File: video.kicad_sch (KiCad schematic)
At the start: 41 parts

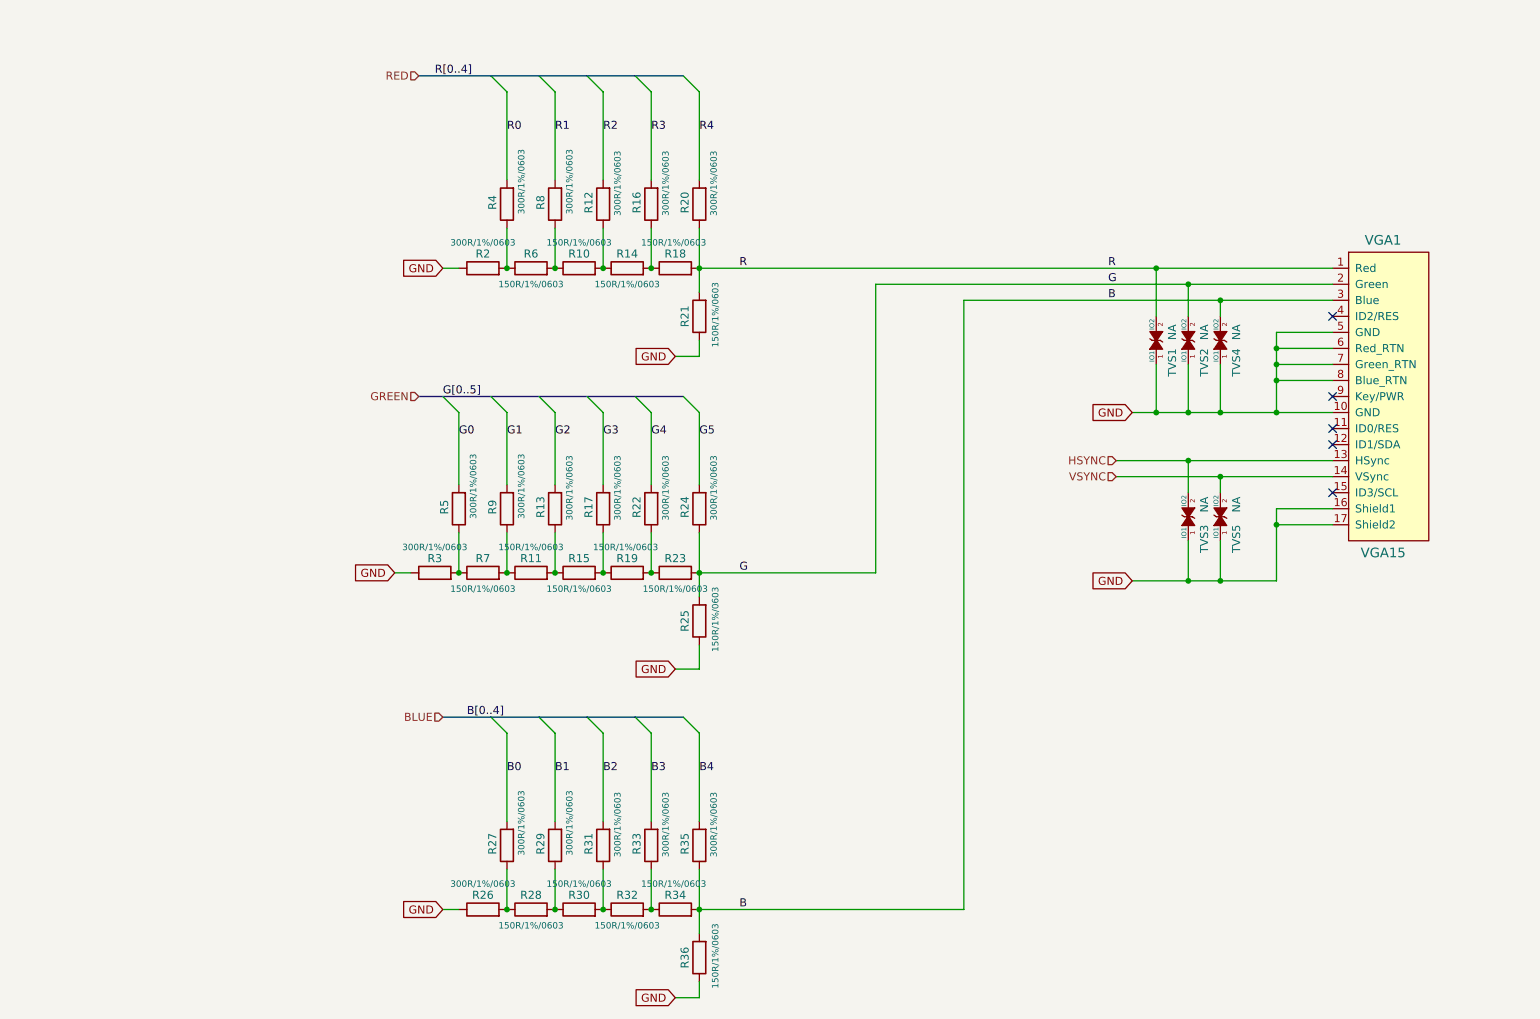
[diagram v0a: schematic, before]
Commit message: schematics finished, pcb routing 80%
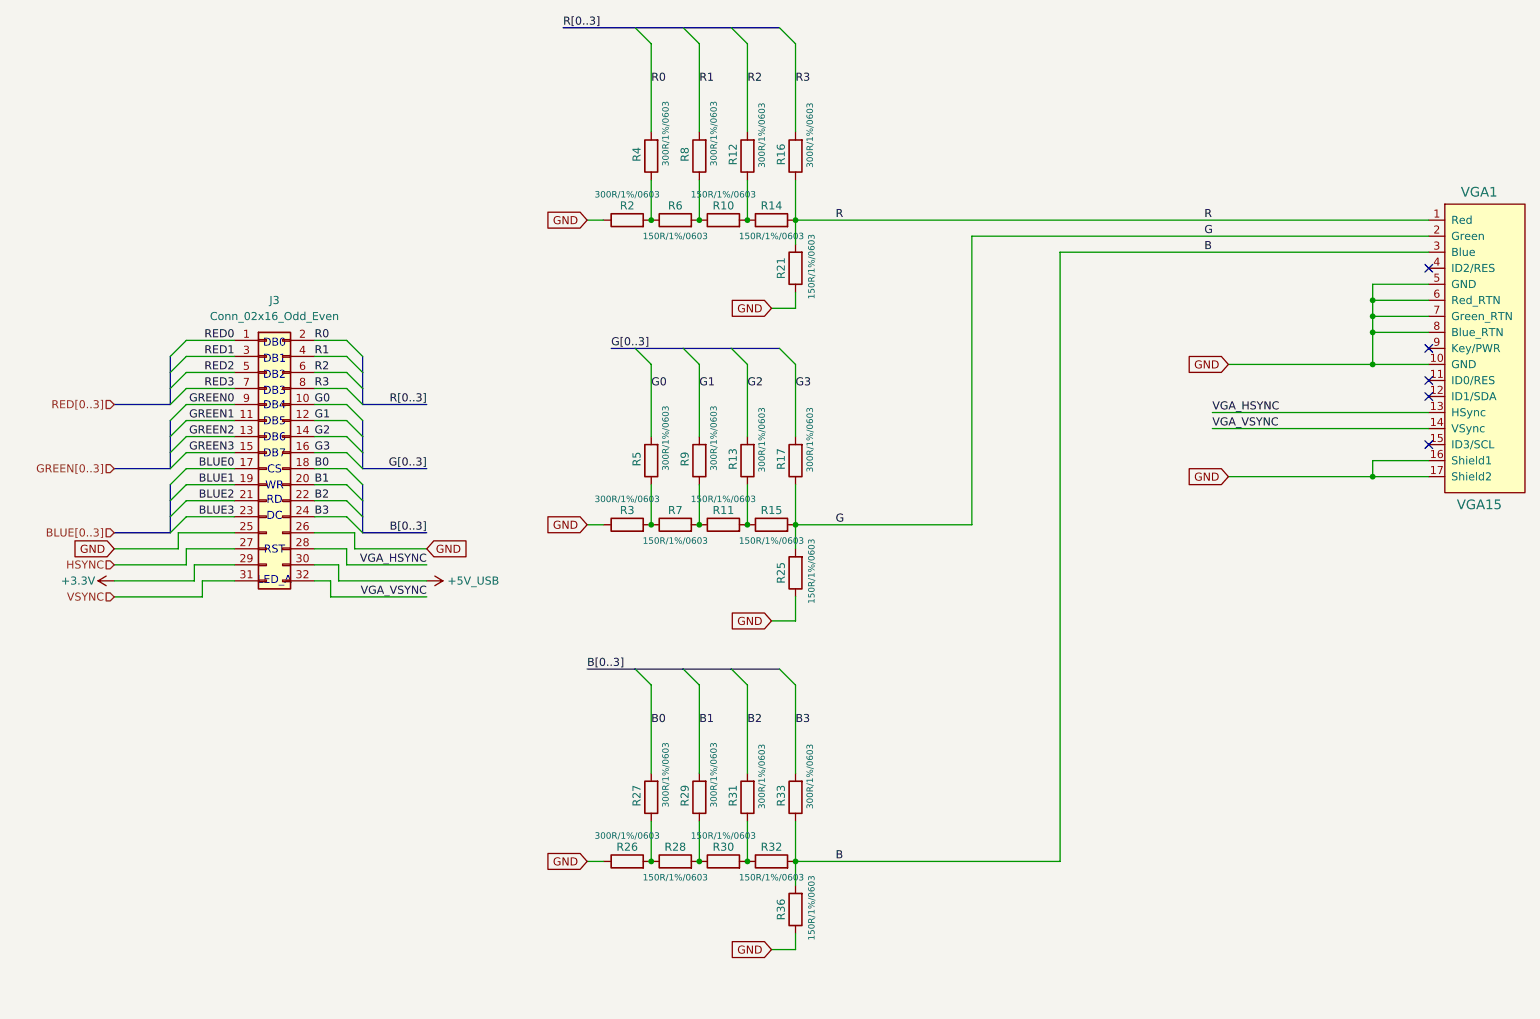
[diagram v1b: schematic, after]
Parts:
- removed R18, R19, R23, R34: 150R/1%/0603, OLIMEX_RLC-FP:R_0603_5MIL_DWS, symbol AgonLight2_Rev_B:R
- removed R20, R22, R24, R35: 300R/1%/0603, OLIMEX_RLC-FP:R_0603_5MIL_DWS, symbol AgonLight2_Rev_B:R
- removed TVS1, TVS2, TVS3, TVS4, TVS5: NA, OLIMEX_Diodes-FP:D_0402_5MIL_DWS, symbol AgonLight2_Rev_B:GG0402052R542P
- added J3: Conn_02x16_Odd_Even, Connector_PinHeader_2.54mm:PinHeader_2x16_P2.54mm_Vertical_SMD, symbol Connector_Generic:Conn_02x16_Odd_Even
- R10, R11, R12, R13, R14, R15, R16, R17, R2, R21, R25, R26, R27, R28, R29, R3, R30, R31, R32, R33, R36, R4, R5, R6, R7, R8, R9: footprint OLIMEX_RLC-FP:R_0603_5MIL_DWS -> HexAgonFootprintsLibrary:R_0603_5MIL_DWS
- VGA1: footprint OLIMEX_Connectors-FP:VGA15-F(CD0515S21J0) -> HexAgonFootprintsLibrary:VGA15-F(CD0515S21J0)
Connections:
- net B: now also R32.2, R33.1
- net B0: now also J3.18 (Pin_18)
- net B1: now also J3.20 (Pin_20)
- net B2: now also J3.22 (Pin_22)
- net B3: now also J3.24 (Pin_24)
- net G: now also R15.2, R17.1
- net G0: now also J3.10 (Pin_10)
- net G1: now also J3.12 (Pin_12)
- net G2: now also J3.14 (Pin_14)
- net G3: now also J3.16 (Pin_16)
- net GND: now also J3.25 (Pin_25), J3.26 (Pin_26)
- net HSYNC: now also J3.27 (Pin_27); no longer VGA1.13 (HSync)
- net R: now also R14.2, R16.1
- net R0: now also J3.2 (Pin_2)
- net R1: now also J3.4 (Pin_4)
- net R2: now also J3.6 (Pin_6)
- net R3: now also J3.8 (Pin_8)
- net VSYNC: now also J3.31 (Pin_31); no longer VGA1.14 (VSync)
- new net +3.3V: J3.29 (Pin_29)
- new net +5V_USB: J3.30 (Pin_30)
- new net BLUE0: J3.17 (Pin_17)
- new net BLUE1: J3.19 (Pin_19)
- new net BLUE2: J3.21 (Pin_21)
- new net BLUE3: J3.23 (Pin_23)
- new net GREEN0: J3.9 (Pin_9)
- new net GREEN1: J3.11 (Pin_11)
- new net GREEN2: J3.13 (Pin_13)
- new net GREEN3: J3.15 (Pin_15)
- new net RED0: J3.1 (Pin_1)
- new net RED1: J3.3 (Pin_3)
- new net RED2: J3.5 (Pin_5)
- new net RED3: J3.7 (Pin_7)
- new net VGA_HSYNC: J3.28 (Pin_28), VGA1.13 (HSync)
- new net VGA_VSYNC: J3.32 (Pin_32), VGA1.14 (VSync)
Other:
- note added: "CS"
- note added: "DB0"
- note added: "DB1"
- note added: "DB2"
- note added: "DB3"
- note added: "DB4"
- note added: "DB5"
- note added: "DB6"
- note added: "DB7"
- note added: "DC"
- note added: "LED_A"
- note added: "RD"
- note added: "RST"
- note added: "WR"
- moved on the sheet: R10, R11, R12, R13, R14, R15, R16, R17, R2, R21, R25, R26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

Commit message: 1st production and BOM
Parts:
- J3: MfgNumber (none) -> 9-146276-0
- R10, R11, R14, R15, R21, R25, R28, R30, R32, R36, R6, R7: MfgNumber (none) -> ERJ-P03F1500V
- R12, R13, R16, R17, R2, R26, R27, R29, R3, R31, R33, R4, R5, R8, R9: MfgNumber (none) -> ERJ-P03F3000V
- VGA1: MfgNumber (none) -> L17HTHES4R1C
